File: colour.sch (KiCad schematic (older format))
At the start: 52 parts, among them J6 Conn_01x07, J7 Conn_02x15_Odd_Even, Q1 BC817, Q2 BC817, Q3 BC817, U6 6116, U7 74LS257, U8 74LS574, U9 74LS257

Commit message: First working version
Hardware validation
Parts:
- added R55, R56, R58, R59: 4k7, Resistor_SMD:R_0805_2012Metric_Pad1.15x1.40mm_HandSolder, symbol Device:R
- R26, R27, R28, R29, R43, R44, R45, R46: value 4k7 -> 2k2
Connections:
- net +5V: now also R55.1, R56.1, R58.1, R59.1
- net INK_B: now also R55.2
- net INK_G: now also R56.2
- net INK_I: now also R59.2
- net INK_R: now also R58.2
- net ~CPAGE renamed CPAGE
- net ~SPAGE renamed SPAGE
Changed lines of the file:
@@
 P 2900 4900
 F 0 "R46" V 2850 5100 50  0000 C CNN
-F 1 "4k7" V 2900 4900 50  0000 C CNN
+F 1 "2k2" V 2900 4900 50  0000 C CNN
 F 2 "Resistor_SMD:R_0805_2012Metric_Pad1.15x1.40mm_HandSolder" V 2830 4900 50  0001 C CNN
 F 3 "~" H 2900 4900 50  0001 C CNN
@@
 P 2800 4900
 F 0 "R45" V 2750 5100 50  0000 C CNN
-F 1 "4k7" V 2800 4900 50  0000 C CNN
+F 1 "2k2" V 2800 4900 50  0000 C CNN
 F 2 "Resistor_SMD:R_0805_2012Metric_Pad1.15x1.40mm_HandSolder" V 2730 4900 50  0001 C CNN
 F 3 "~" H 2800 4900 50  0001 C CNN
@@
 P 2700 4900
 F 0 "R44" V 2650 5100 50  0000 C CNN
-F 1 "4k7" V 2700 4900 50  0000 C CNN
+F 1 "2k2" V 2700 4900 50  0000 C CNN
 F 2 "Resistor_SMD:R_0805_2012Metric_Pad1.15x1.40mm_HandSolder" V 2630 4900 50  0001 C CNN
 F 3 "~" H 2700 4900 50  0001 C CNN
@@
 P 2600 4900
 F 0 "R43" V 2550 5100 50  0000 C CNN
-F 1 "4k7" V 2600 4900 50  0000 C CNN
+F 1 "2k2" V 2600 4900 50  0000 C CNN
 F 2 "Resistor_SMD:R_0805_2012Metric_Pad1.15x1.40mm_HandSolder" V 2530 4900 50  0001 C CNN
 F 3 "~" H 2600 4900 50  0001 C CNN
@@
 P 8000 4550
 F 0 "R26" V 8050 4350 50  0000 C CNN
-F 1 "4k7" V 8000 4550 50  0000 C CNN
+F 1 "2k2" V 8000 4550 50  0000 C CNN
 F 2 "Resistor_SMD:R_0805_2012Metric_Pad1.15x1.40mm_HandSolder" V 7930 4550 50  0001 C CNN
 F 3 "~" H 8000 4550 50  0001 C CNN
@@
 P 8200 4550
 F 0 "R27" V 8250 4350 50  0000 C CNN
-F 1 "4k7" V 8200 4550 50  0000 C CNN
+F 1 "2k2" V 8200 4550 50  0000 C CNN
 F 2 "Resistor_SMD:R_0805_2012Metric_Pad1.15x1.40mm_HandSolder" V 8130 4550 50  0001 C CNN
 F 3 "~" H 8200 4550 50  0001 C CNN
@@
 P 8400 4550
 F 0 "R28" V 8450 4350 50  0000 C CNN
-F 1 "4k7" V 8400 4550 50  0000 C CNN
+F 1 "2k2" V 8400 4550 50  0000 C CNN
 F 2 "Resistor_SMD:R_0805_2012Metric_Pad1.15x1.40mm_HandSolder" V 8330 4550 50  0001 C CNN
 F 3 "~" H 8400 4550 50  0001 C CNN
@@
 P 8600 4550
 F 0 "R29" V 8650 4350 50  0000 C CNN
-F 1 "4k7" V 8600 4550 50  0000 C CNN
+F 1 "2k2" V 8600 4550 50  0000 C CNN
 F 2 "Resistor_SMD:R_0805_2012Metric_Pad1.15x1.40mm_HandSolder" V 8530 4550 50  0001 C CNN
 F 3 "~" H 8600 4550 50  0001 C CNN
@@
 	4950 6250 5050 6250
 Text Label 5650 6350 0    60   ~ 0
-~SPAGE
+SPAGE
 Wire Wire Line
 	5550 6350 6050 6350
@@
 ~VRAMWR
 Text Label 950  2200 2    60   ~ 0
-~SPAGE
+SPAGE
 Text Label 950  2600 2    50   ~ 0
 ~SCRRAM
 Text GLabel 6050 6350 2    50   Input ~ 0
-~SPAGE
+SPAGE
 Text GLabel 4500 6350 0    50   Input ~ 0
-~CPAGE
+CPAGE
 Wire Wire Line
 	4900 2600 5500 2600
@@
 Wire Wire Line
 	12700 3650 12950 3650
+$Comp
+L Device:R R55
+U 1 1 5F2AF835
+P 3650 5450
+F 0 "R55" V 3650 5800 50  0000 C CNN
+F 1 "4k7" V 3650 5450 50  0000 C CNN
+F 2 "Resistor_SMD:R_0805_2012Metric_Pad1.15x1.40mm_HandSolder" V 3580 5450 50  0001 C CNN
+F 3 "~" H 3650 5450 50  0001 C CNN
+	1    3650 5450
+	0    1    1    0
+$EndComp
+$Comp
+L Device:R R56
+U 1 1 5F2B0862
+P 3650 5550
+F 0 "R56" V 3650 5900 50  0000 C CNN
+F 1 "4k7" V 3650 5550 50  0000 C CNN
+F 2 "Resistor_SMD:R_0805_2012Metric_Pad1.15x1.40mm_HandSolder" V 3580 5550 50  0001 C CNN
+F 3 "~" H 3650 5550 50  0001 C CNN
+	1    3650 5550
+	0    1    1    0
+$EndComp
+$Comp
+L Device:R R58
+U 1 1 5F2B0A96
+P 3650 5650
+F 0 "R58" V 3650 6000 50  0000 C CNN
+F 1 "4k7" V 3650 5650 50  0000 C CNN
+F 2 "Resistor_SMD:R_0805_2012Metric_Pad1.15x1.40mm_HandSolder" V 3580 5650 50  0001 C CNN
+F 3 "~" H 3650 5650 50  0001 C CNN
+	1    3650 5650
+	0    1    1    0
+$EndComp
+$Comp
+L Device:R R59
+U 1 1 5F2B0C2A
+P 3650 5750
+F 0 "R59" V 3650 6100 50  0000 C CNN
+F 1 "4k7" V 3650 5750 50  0000 C CNN
+F 2 "Resistor_SMD:R_0805_2012Metric_Pad1.15x1.40mm_HandSolder" V 3580 5750 50  0001 C CNN
+F 3 "~" H 3650 5750 50  0001 C CNN
+	1    3650 5750
+	0    1    1    0
+$EndComp
+Wire Wire Line
+	3500 5450 3400 5450
+Connection ~ 3400 5450
+Wire Wire Line
+	3500 5550 3300 5550
+Connection ~ 3300 5550
+Wire Wire Line
+	3500 5650 3200 5650
+Connection ~ 3200 5650
+Wire Wire Line
+	3500 5750 3100 5750
+Connection ~ 3100 5750
+Wire Wire Line
+	3800 5750 3900 5750
+Wire Wire Line
+	3900 5750 3900 5650
+Wire Wire Line
+	3800 5450 3900 5450
+Connection ~ 3900 5450
+Wire Wire Line
+	3900 5450 3900 5300
+Wire Wire Line
+	3800 5550 3900 5550
+Connection ~ 3900 5550
+Wire Wire Line
+	3900 5550 3900 5450
+Wire Wire Line
+	3800 5650 3900 5650
+Connection ~ 3900 5650
+Wire Wire Line
+	3900 5650 3900 5550
+$Comp
+L power:+5V #PWR039
+U 1 1 5F33F5FA
+P 3900 5300
+F 0 "#PWR039" H 3900 5150 50  0001 C CNN
+F 1 "+5V" H 3915 5473 50  0000 C CNN
+F 2 "" H 3900 5300 50  0001 C CNN
+F 3 "" H 3900 5300 50  0001 C CNN
+	1    3900 5300
+	1    0    0    -1
+$EndComp
 $EndSCHEMATC

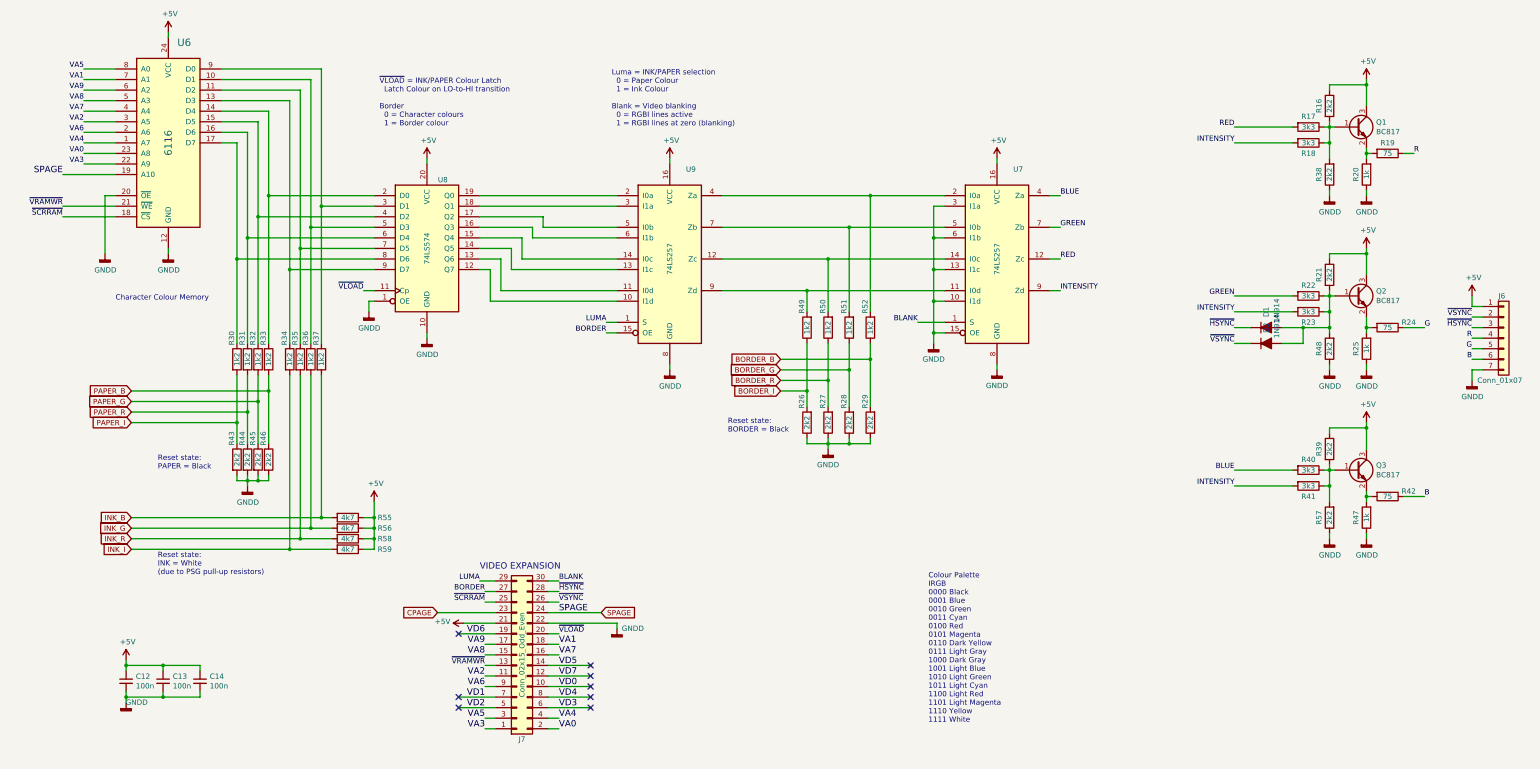
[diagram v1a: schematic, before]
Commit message: Text corrections
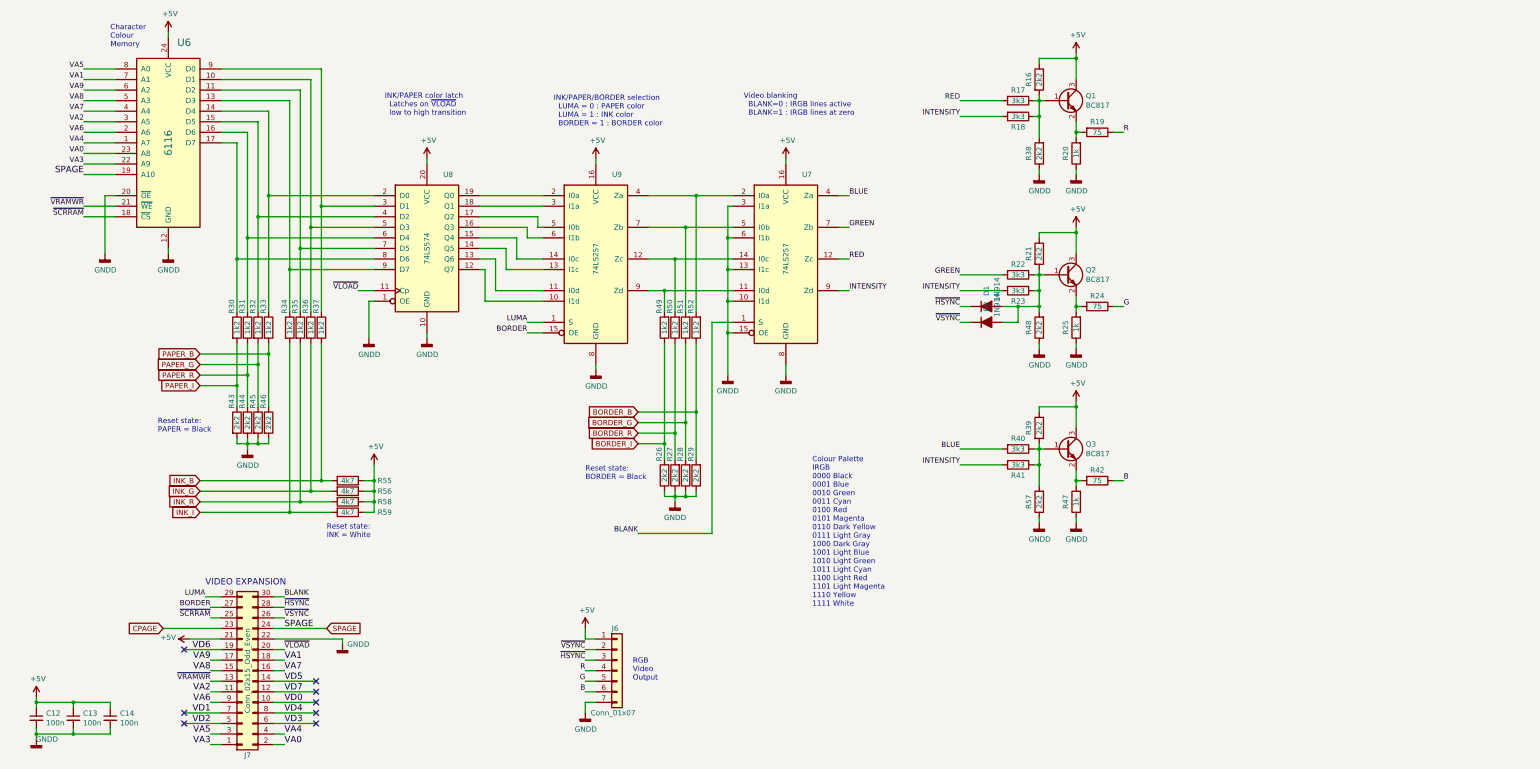
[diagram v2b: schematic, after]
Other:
- note added: "Character\nColour\nMemory"
- note added: "INK/PAPER color latch\n Latches on ~VLOAD~\n low to high transition"
- note added: "INK/PAPER/BORDER selection\n LUMA = 0 : PAPER color\n LUMA = 1 : INK color\n BORDER = 1 : BORDER color"
- note added: "RGB\nVideo\nOutput"
- note added: "Reset state:\nINK = White"
- note added: "Video blanking\n BLANK=0 : IRGB lines active\n BLANK=1 : IRGB lines at zero"
- note removed: "Character Colour Memory"
- note removed: "Luma = INK/PAPER selection\n 0 = Paper Colour\n 1 = Ink Colour\n\nBlank = Video blanking\n 0 = RGBI lines active\n 1 = RGBI lines at zero (blanking)"
- note removed: "Reset state:\nINK = White\n(due to PSG pull-up resistors)"
- note removed: "~VLOAD~ = INK/PAPER Colour Latch\n Latch Colour on LO-to-HI transition\n\nBorder\n 0 = Character colours\n 1 = Border colour"
- moved on the sheet: C12, C13, C14, D1, D2, J6, J7, Q1, Q2, Q3, R16, R17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
